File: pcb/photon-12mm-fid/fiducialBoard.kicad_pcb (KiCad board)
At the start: 2 copper layers, 12 x 4 mm, 3 parts

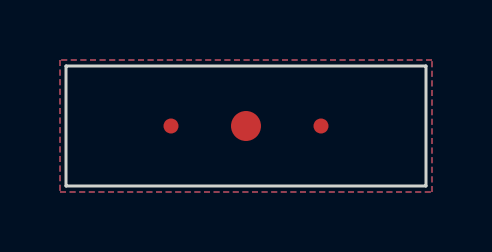
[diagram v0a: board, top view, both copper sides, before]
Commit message: uprevs 12mm fid to rev01 to have little silkscreen corners
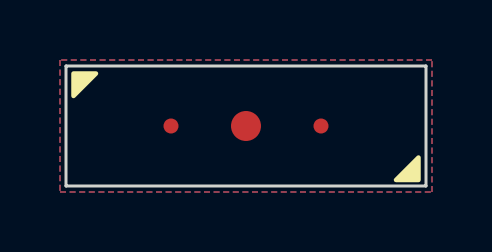
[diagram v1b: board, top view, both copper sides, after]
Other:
- board text added: "12mm Fiducial REV01"
- board text removed: "12mm Fiducial REV00"
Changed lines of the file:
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@@
       (solder_mask_margin 0.5) (clearance 0.5))
   )
+  (gr_poly
+    (pts
+      (xy 0.25 -3.75)
+      (xy 0.25 -3)
+      (xy 1 -3.75)
+    )
+    (stroke (width 0.15) (type solid)) (fill solid) (layer "F.SilkS"))
+  (gr_poly
+    (pts
+      (xy 11.75 -0.2)
+      (xy 11.75 -0.95)
+      (xy 11 -0.2)
+    )
+    (stroke (width 0.15) (type solid)) (fill solid) (layer "F.SilkS"))
   (gr_line (start 0 0) (end 12 0)
     (stroke (width 0.1) (type solid)) (layer "Edge.Cuts"))
@@
   (gr_line (start 12 0) (end 12 -4)
     (stroke (width 0.1) (type solid)) (layer "Edge.Cuts"))
-  (gr_text "12mm Fiducial\nREV00" (at 6 -2) (layer "B.SilkS")
+  (gr_text "12mm Fiducial\nREV01" (at 6 -2) (layer "B.SilkS")
     (effects (font (size 0.75 0.75) (thickness 0.1)) (justify mirror))
   )
